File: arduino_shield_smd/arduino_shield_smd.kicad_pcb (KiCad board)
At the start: 2 copper layers, 68.6 x 53.3 mm, 51 parts, among them J1 Power, J2 Digital/PWM, J3 Analog, J4 Digital/PWM, J5 1X5 2.5mm, J6 1x2 2.5mm, U1 PCF8574T, U2 ULN2803A, U3 PCF8574T, U4 ULN2803A

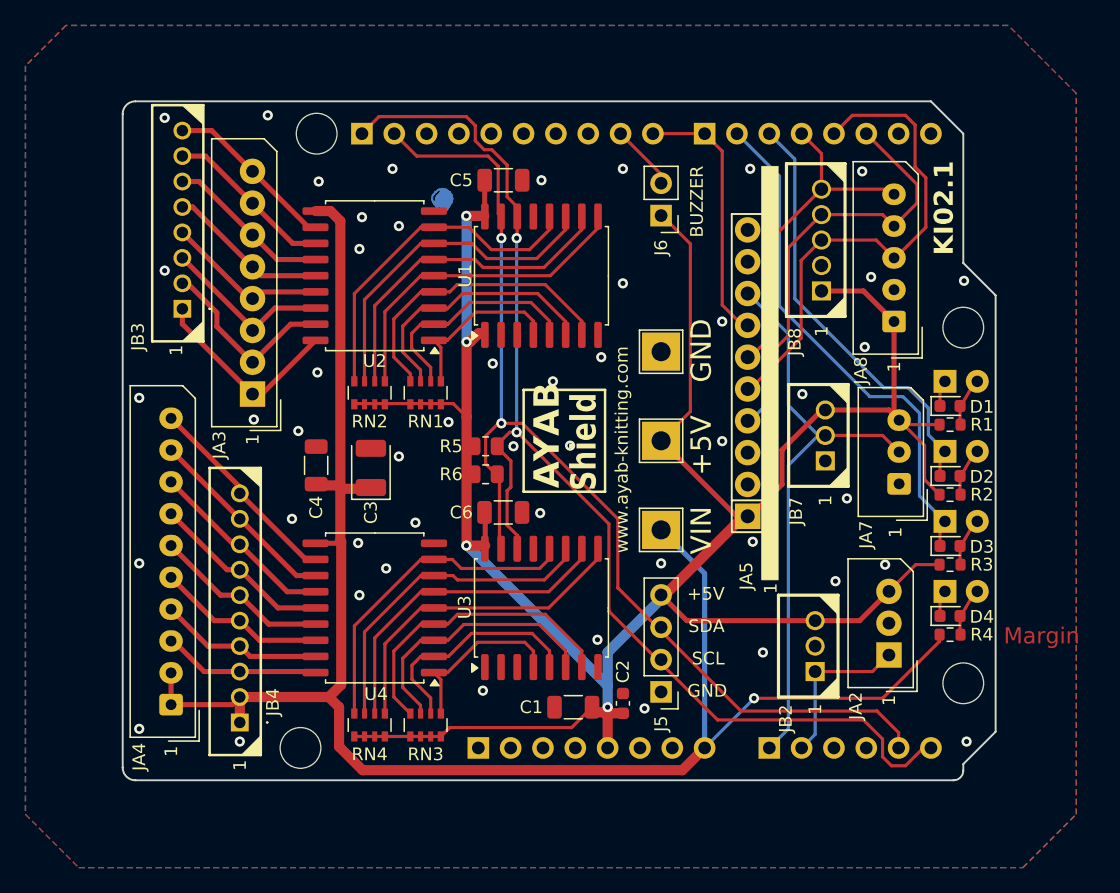
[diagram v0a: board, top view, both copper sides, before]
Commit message: Rename knitting machine connectors and fix schematic for EOL connectors
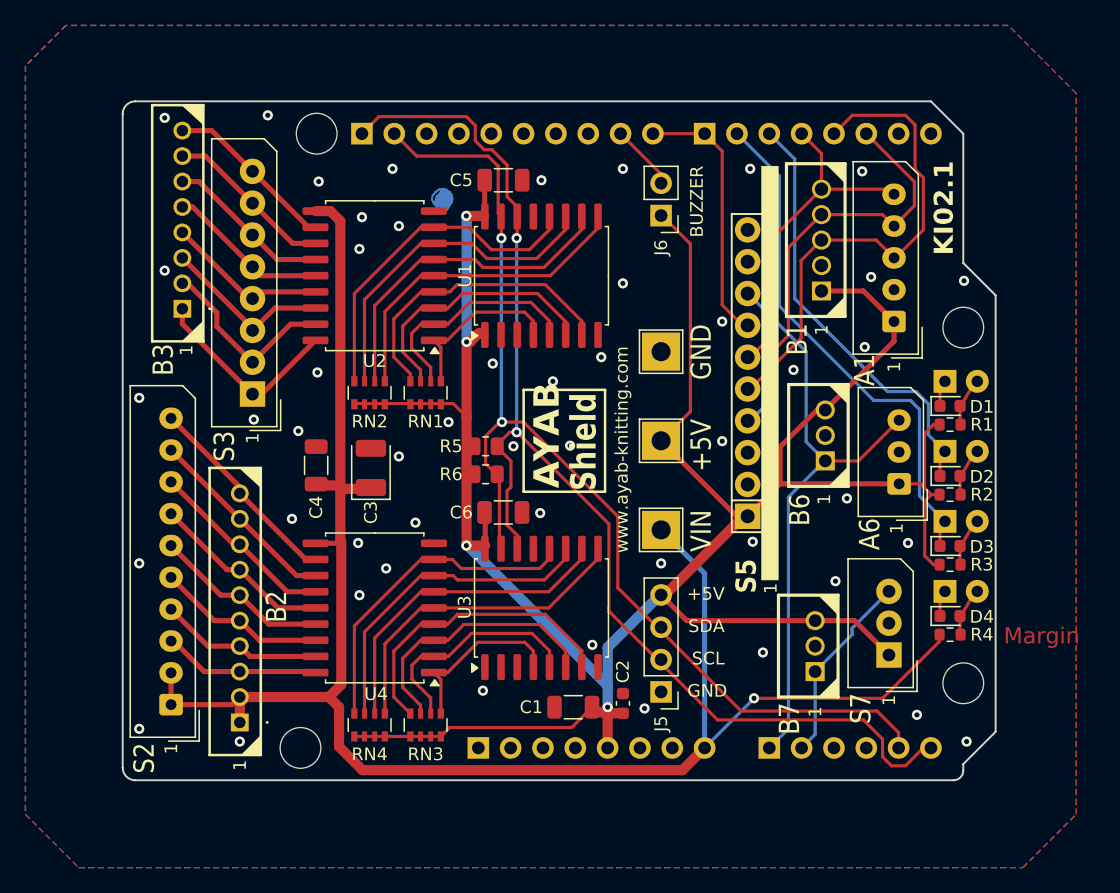
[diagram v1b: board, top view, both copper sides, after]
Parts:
- renumbered JA8 to A1, JA7 to A6, JB8 to B1, JB4 to B2, JB3 to B3, JB7 to B6, JB2 to B7, JA4 to S2, JA3 to S3, JA5 to S5, JA2 to S7
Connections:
- A6 pad 1: GND -> +5V
- A6 pad 2: /EOL_R -> GND
- A6 pad 3: +5V -> /EOL_R
- B6 pad 1: GND -> /EOL_R
- B6 pad 2: /EOL_R -> GND
- S5 pad 10: /MYLAR2 -> unconnected-(S5-Pin_10-Pad10)
- S5 pad 9: /MYLAR1 -> unconnected-(S5-Pin_9-Pad9)
- S7 pad 1: /EOL_L -> +5V
- S7 pad 3: +5V -> /EOL_L
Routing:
- net +5V: track 202.0 -> 208.7 mm
- net /EOL_L: track 12.8 -> 15.1 mm
- net /EOL_R: track 46.7 -> 47.8 mm
- net GND: track 0.02 -> 0.43 mm, vias 49 -> 50

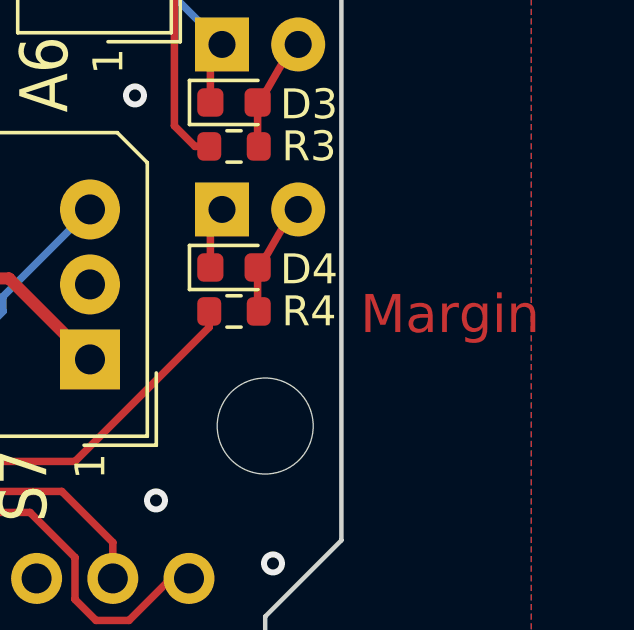
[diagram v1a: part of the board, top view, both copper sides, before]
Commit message: Connect S5.9 and S5.10 to GND
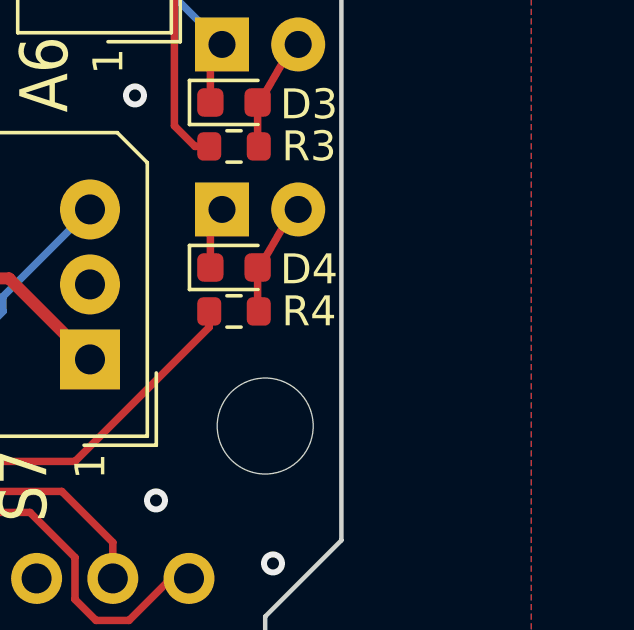
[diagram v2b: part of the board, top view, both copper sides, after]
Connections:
- S5 pad 10: unconnected-(S5-Pin_10-Pad10) -> GND
- S5 pad 9: unconnected-(S5-Pin_9-Pad9) -> GND
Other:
- board text removed: "Margin"

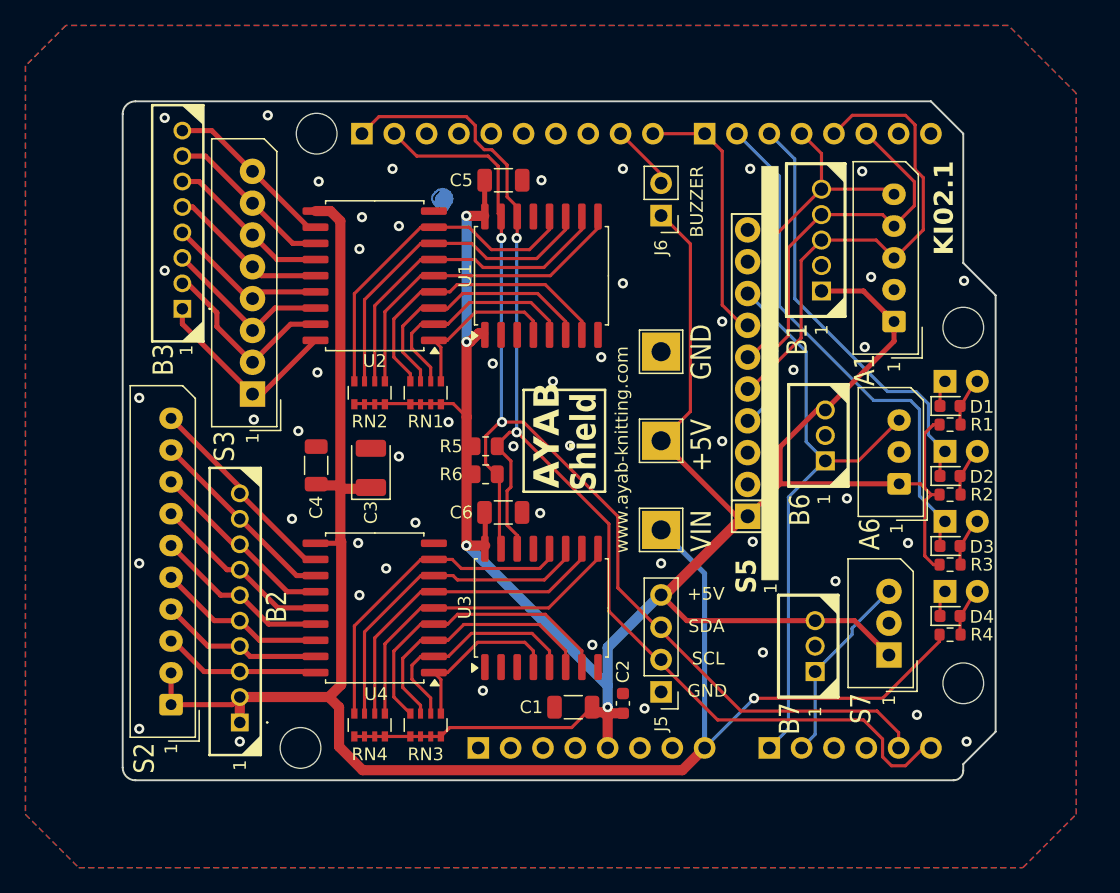
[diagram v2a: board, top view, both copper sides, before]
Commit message: Fix 2mm pitch 5-pin connector pinout
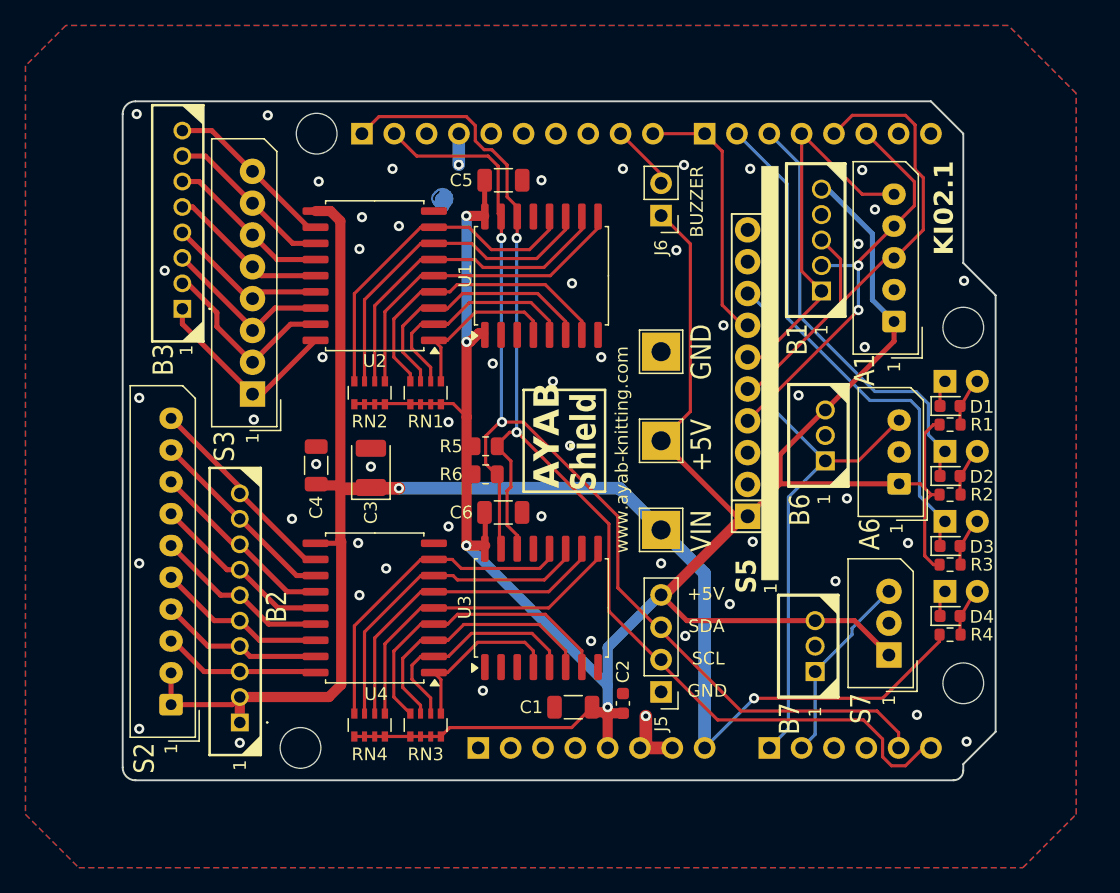
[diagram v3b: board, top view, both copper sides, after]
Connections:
- B1 pad 1: +5V -> /ENC_C
- B1 pad 2: GND -> /ENC_A
- B1 pad 4: /ENC_A -> GND
- B1 pad 5: /ENC_C -> +5V
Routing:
- net VIN: track 139.3 -> 129.0 mm, vias 1 -> 2
- net GND: track 0.43 -> 8.08 mm, vias 50 -> 53
- net +5V: track 208.7 -> 214.2 mm
- net /ENC_C: track 26.5 -> 31.6 mm
- net /ENC_A: track 34.1 -> 32.5 mm, vias 1 -> 2
- net /ENC_B: track 39.3 -> 40.3 mm
- net /LED_YEL: track 32.4 -> 33.0 mm

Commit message: Fix pinout for solenoid headers
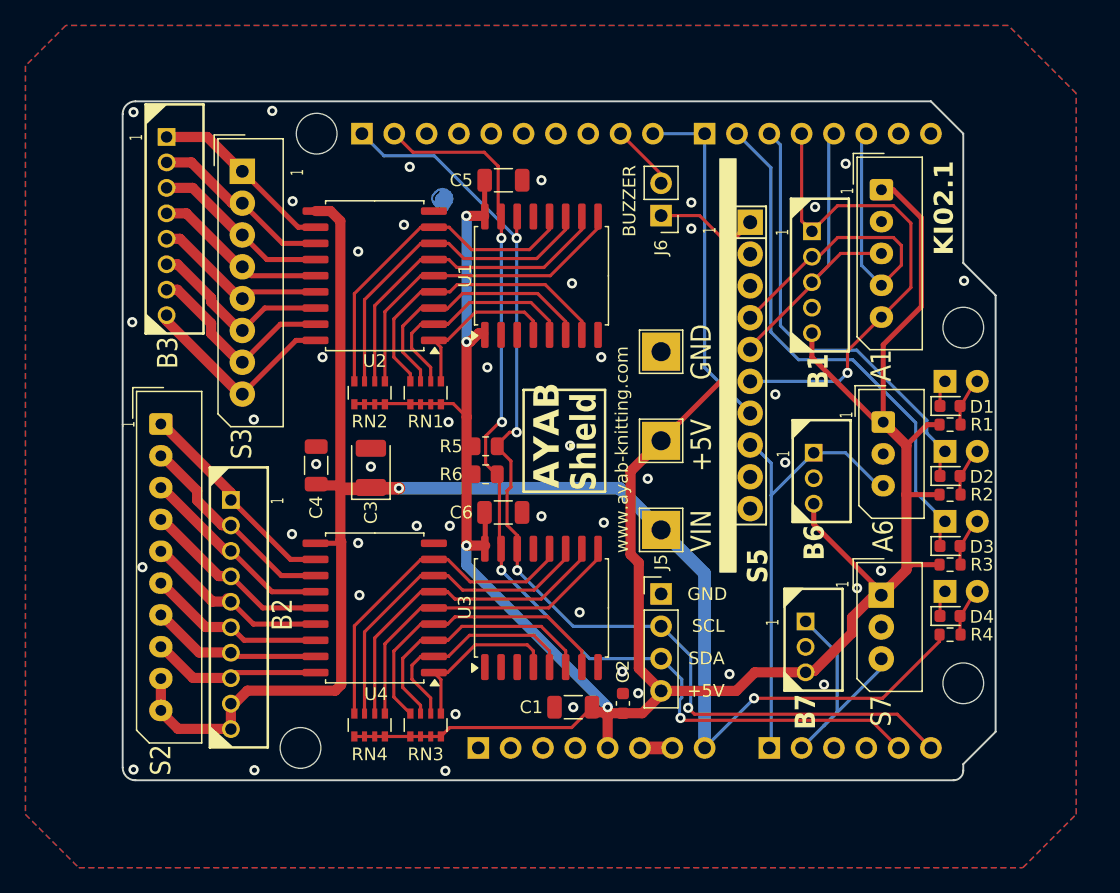
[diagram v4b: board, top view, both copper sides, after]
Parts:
- B1: footprint ayab-library:CONN-TH_A2004WV-5P -> ayab-library:530140510
- B6, B7: footprint ayab-library:CONN-TH_3P-P2.00_A2004WV-3P -> ayab-library:530140310
- moved S5 23.1 mm to (164.0, 86.2), turned to -90 degrees
- moved S2 22.1 mm to (117.7, 102.0), turned to -90 degrees
- moved S3 17.5 mm to (124.1, 82.2), turned to -90 degrees
- moved B2 17.5 mm to (123.2, 108.0), turned to 90 degrees
- moved B3 13.6 mm to (118.2, 79.5), turned to 90 degrees
- moved A1 10.4 mm to (174.3, 83.7), turned to -90 degrees
- moved J5 7.70 mm to (157.0, 115.4), turned to 0 degrees
- moved A6 5.01 mm to (174.4, 101.9), turned to -90 degrees
- moved S7 4.74 mm to (174.3, 115.5), turned to -90 degrees
- moved B7 2.08 mm to (168.3, 117.6), turned to 90 degrees
- moved B6 1.64 mm to (169.0, 104.3), turned to 90 degrees
- moved B1 1.02 mm to (168.8, 86.9), turned to 90 degrees
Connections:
- B2 pad 1: VIN -> Net-(B2-Pin_1)
- B2 pad 10: Net-(B2-Pin_10) -> VIN
- B2 pad 2: VIN -> Net-(B2-Pin_2)
- B2 pad 9: Net-(B2-Pin_9) -> VIN
- S2 pad 1: VIN -> Net-(B2-Pin_1)
- S2 pad 10: Net-(B2-Pin_10) -> VIN
- S2 pad 2: VIN -> Net-(B2-Pin_2)
- S2 pad 9: Net-(B2-Pin_9) -> VIN
- U2 pad 11: Net-(B3-Pin_8) -> Net-(B3-Pin_1)
- U2 pad 12: Net-(B3-Pin_7) -> Net-(B3-Pin_2)
- U2 pad 13: Net-(B3-Pin_6) -> Net-(B3-Pin_3)
- U2 pad 14: Net-(B3-Pin_5) -> Net-(B3-Pin_4)
- U2 pad 15: Net-(B3-Pin_4) -> Net-(B3-Pin_5)
- U2 pad 16: Net-(B3-Pin_3) -> Net-(B3-Pin_6)
- U2 pad 17: Net-(B3-Pin_2) -> Net-(B3-Pin_7)
- U2 pad 18: Net-(B3-Pin_1) -> Net-(B3-Pin_8)
- U4 pad 11: Net-(B2-Pin_10) -> Net-(B2-Pin_1)
- U4 pad 12: Net-(B2-Pin_9) -> Net-(B2-Pin_2)
- U4 pad 13: Net-(B2-Pin_8) -> Net-(B2-Pin_3)
- U4 pad 14: Net-(B2-Pin_7) -> Net-(B2-Pin_4)
- U4 pad 15: Net-(B2-Pin_6) -> Net-(B2-Pin_5)
- U4 pad 16: Net-(B2-Pin_5) -> Net-(B2-Pin_6)
- U4 pad 17: Net-(B2-Pin_4) -> Net-(B2-Pin_7)
- U4 pad 18: Net-(B2-Pin_3) -> Net-(B2-Pin_8)
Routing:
- net Net-(B2-Pin_1): track 0.00 -> 16.9 mm
- net Net-(B2-Pin_2): track 0.00 -> 16.5 mm
- net Net-(B2-Pin_10): track 16.2 -> 0.00 mm
- net Net-(B2-Pin_9): track 15.4 -> 0.00 mm
- net /ENC_B: track 40.3 -> 26.1 mm
- net /EOL_R: track 47.8 -> 35.9 mm
- net +5V: track 214.2 -> 225.4 mm
- net /SCL: track 95.3 -> 86.6 mm, vias 2 -> 4
- net /ENC_C: track 31.6 -> 38.9 mm, vias 0 -> 1
- net /910_L: track 20.8 -> 27.5 mm
- net GND: track 8.08 -> 2.56 mm, vias 53 -> 45
- net /SDA: track 86.1 -> 81.5 mm, vias 2 -> 4
- net /EOL_L: track 15.1 -> 19.3 mm
- net Net-(B2-Pin_3): track 12.6 -> 15.5 mm
- net Net-(B3-Pin_8): track 13.6 -> 16.3 mm
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
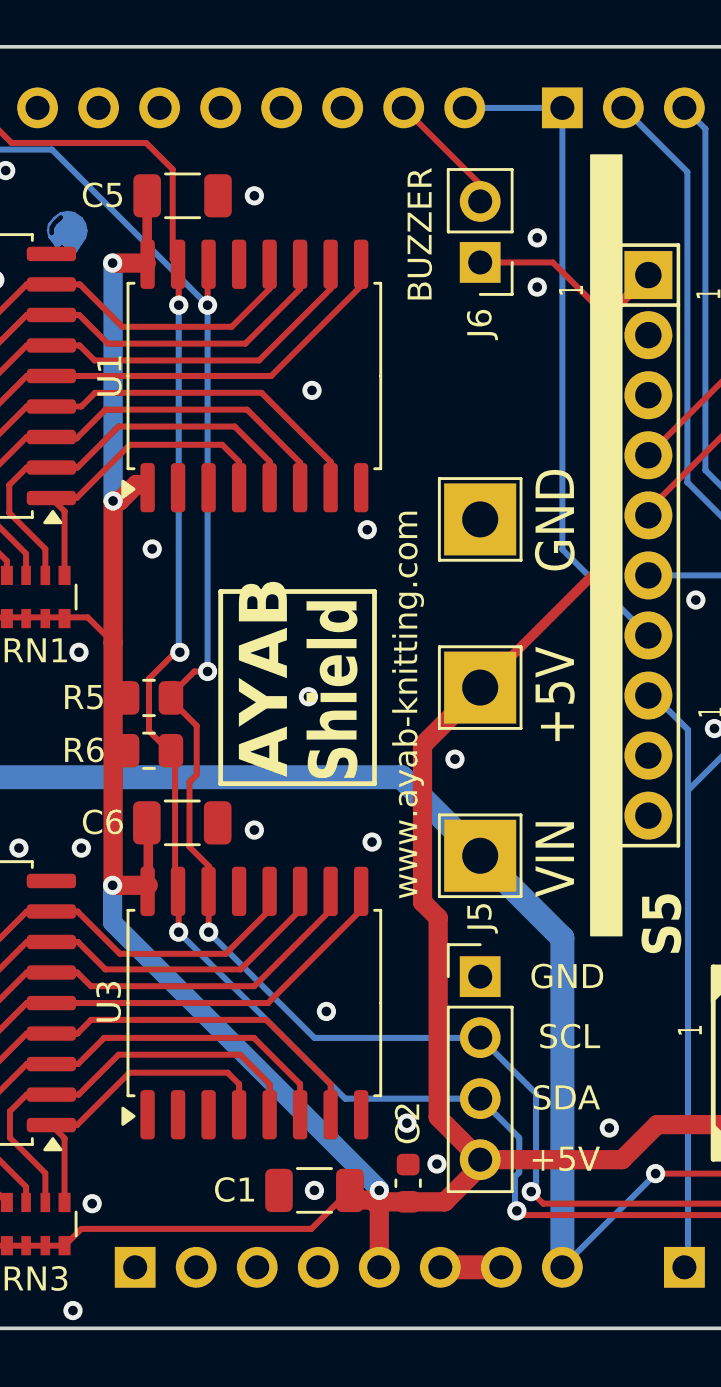
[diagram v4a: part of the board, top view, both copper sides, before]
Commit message: Tweak top silkscreen
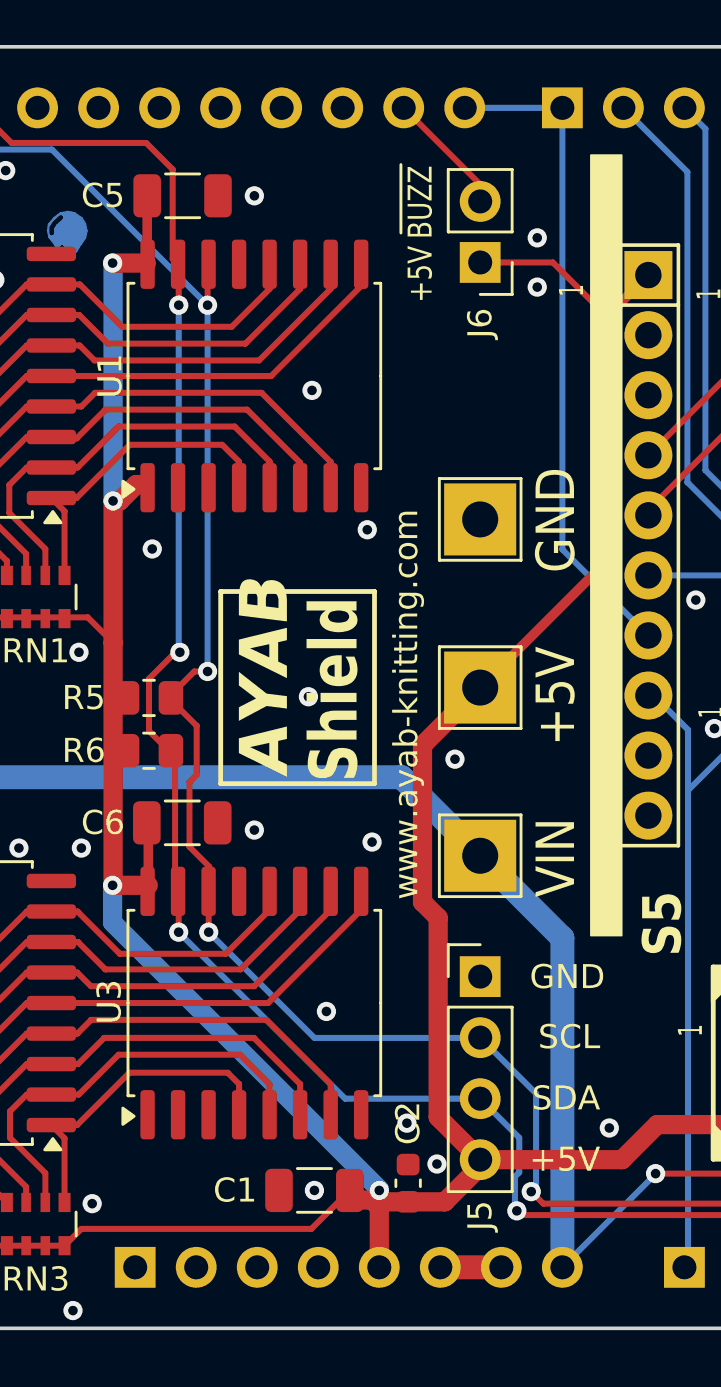
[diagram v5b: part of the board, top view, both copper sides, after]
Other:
- board text added: "BUZZ"
- board text removed: "BUZZER"
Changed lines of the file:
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@@
 		(tags "Through hole pin header THT 1x04 2.54mm single row")
 		(property "Reference" "J5"
-			(at 0 -2.5 90)
+			(at 0 9.95 90)
 			(layer "F.SilkS")
 			(effects
@@
 	)
 	(gr_line
+		(start 153.7 84.45)
+		(end 153.7 81.6)
+		(stroke
+			(width 0.12)
+			(type solid)
+		)
+		(layer "F.SilkS")
+	)
+	(gr_line
 		(start 108.35 86.225)
 		(end 124.225 86.225)
@@
 				(thickness 0.36)
 				(bold yes)
+				(italic yes)
 			)
 			(justify left bottom)
@@
 		)
 	)
+	(gr_text "+5V"
+		(at 155.1 87.35 90)
+		(layer "F.SilkS")
+		(effects
+			(font
+				(size 1 0.8)
+				(thickness 0.125)
+			)
+			(justify left bottom)
+		)
+	)
 	(gr_text "www.ayab-knitting.com"
 		(at 154.5 112.2 90)
@@
 		)
 	)
-	(gr_text "BUZZER"
-		(at 155.1 87.35 90)
+	(gr_text "BUZZ"
+		(at 155.1 84.7 90)
 		(layer "F.SilkS")
 		(effects
 			(font
-				(size 1 1)
+				(size 1 0.8)
 				(thickness 0.125)
 			)
